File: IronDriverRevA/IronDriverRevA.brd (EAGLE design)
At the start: 100 x 100 mm, 46 parts, among them IC1 PIC18F2550, IC2 TL074P, IC3 7805TV, IC4 TL072P, IC5 MC34063AP, Q1 BC557C

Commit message: Finalizando Roteamento
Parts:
- added JMP1, JMP2, JMP3, JMP4, JMP5, JMP6, JMP7: (no value), rcl:R1206
- moved R9 26.6 mm to (60.7, 51.3), turned to 270 degrees
- moved ICSP 17.9 mm to (78.8, 56.0)
- moved R8 15.0 mm to (51.4, 37.1)
- moved IC2 15.0 mm to (51.4, 47.9)
- moved R10 14.4 mm to (60.7, 41.6)
- moved R7 14.4 mm to (58.1, 46.6)
- moved J1 14.2 mm to (90.6, 33.0)
- moved C1 13.4 mm to (85.6, 30.0)
- moved IC1 13.1 mm to (78.8, 35.0)
- moved R6 13.1 mm to (69.7, 47.8)
- moved R5 11.0 mm to (47.6, 25.0), turned to 270 degrees
- moved R3 7.94 mm to (50.1, 25.0), turned to 90 degrees
- moved PTC 7.03 mm to (5.85, 46.0)
- moved IC4 7.03 mm to (23.0, 51.0)
- moved Q1 7.03 mm to (34.5, 51.2)
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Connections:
- removed net LCD_D4: IC1.3
- removed net LCD_D5: IC1.5
- removed net LCD_D6: IC1.6
- removed net LCD_D7: IC1.7
- new net +5V_JMP4: J1.P$5, JMP4.1, R6.2
- new net +5V_MC: C1.1, IC1.20, JMP3.1
- new net GND_JMP5: J1.P$3, JMP5.1
- new net N$17: J1.P$6, JMP1.2
- new net N$23: J1.P$9, JMP7.2
- new net N$24: JMP6.2, JMP7.1
- new net ZEROCROSSING_B: JMP2.1, OPTO1.5, OPTO2.5, R3.1
- net +5V: now also JMP3.2, JMP4.2; no longer C1.1, IC1.20, J1.P$5, R6.2
- net ENC_B: now also JMP1.1; no longer J1.P$6
- net GND: now also JMP5.2; no longer J1.P$3
- net LCD_BL: now also IC1.25
- net LCD_D0: now also IC1.12
- net LCD_D1: now also IC1.17
- net LCD_D2: now also IC1.3
- net LCD_D3: now also IC1.26, JMP6.1; no longer J1.P$9
- net LCD_E: now also IC1.13; no longer IC1.18
- net LCD_RS: now also IC1.24; no longer IC1.17
- net LCD_RW: now also IC1.18; no longer IC1.13
- net ZEROCROSSING: now also JMP2.2; no longer OPTO1.5, OPTO2.5, R3.1
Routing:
- net GND: track 336.0 -> 413.4 mm
- net +5V: track 10.9 -> 63.3 mm
- net +5V_JMP4: track 0.00 -> 42.4 mm
- net LCD_D2: track 0.00 -> 40.0 mm
- net ZEROCROSSING_B: track 0.00 -> 33.7 mm
- net HEATER: track 0.00 -> 29.9 mm
- net ZEROCROSSING: track 18.1 -> 44.6 mm
- net GND_JMP5: track 0.00 -> 24.4 mm
- net LCD_D3: track 0.00 -> 21.2 mm
- net +PTC: track 55.4 -> 75.7 mm
- net LCD_E: track 0.00 -> 20.2 mm
- net LCD_D0: track 0.00 -> 19.0 mm
- net ENC_B: track 22.2 -> 4.09 mm
- net N$6: track 24.5 -> 7.59 mm
- net LCD_RW: track 24.6 -> 8.48 mm
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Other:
- board size 100 x 100 mm -> 100 x 60 mm
- board text added: "10/2014"
- board text added: "IronDriver"
- board text added: "Iuri C."
- board text added: "RevA"
- board text removed: "Subir MOC e OPTOS"

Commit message: Ajustes de trilhas
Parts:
- L2: device rcl:6000-XXXX-RC -> rcl:0204/7
- moved L2 1.35 mm to (66.5, 19.2), turned to 270 degrees
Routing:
- net N$16: track 18.0 -> 24.1 mm
- net +8V: track 132.7 -> 128.1 mm
- net GND: track 413.4 -> 412.4 mm
- net +5V: track 63.3 -> 62.5 mm

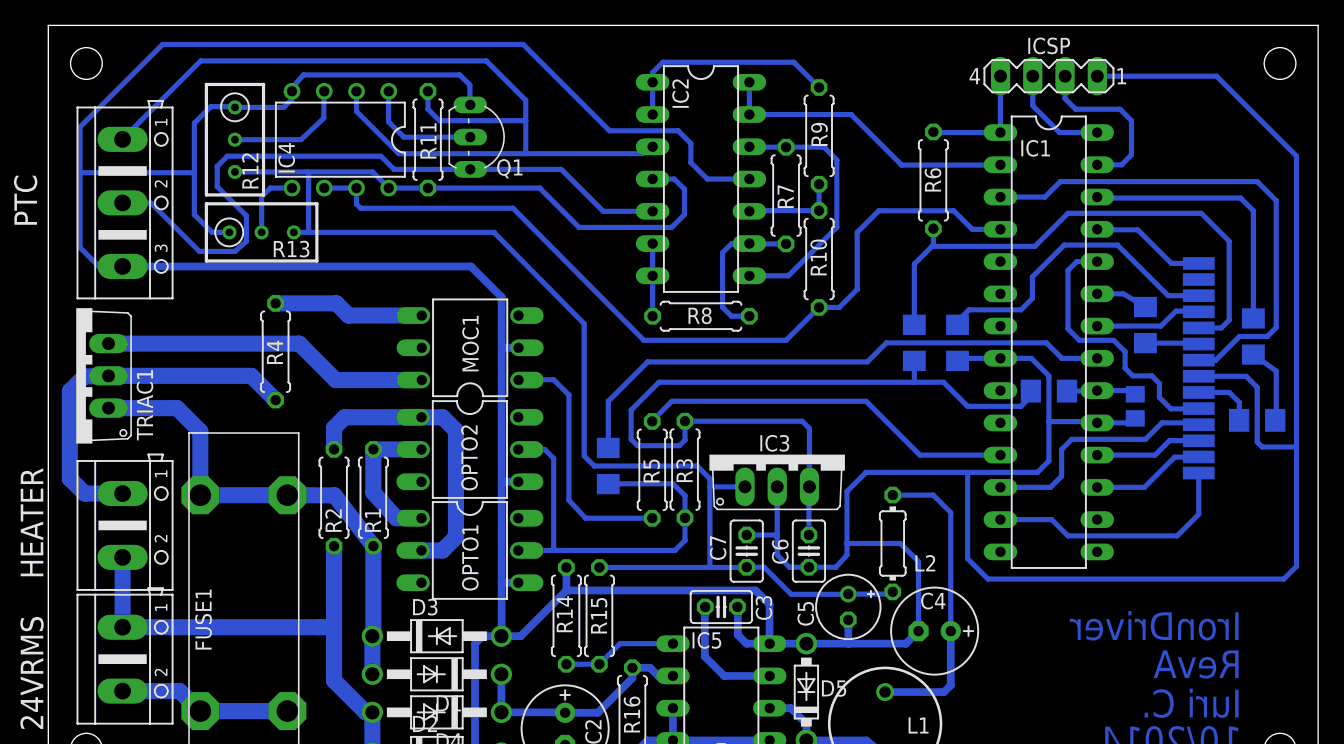
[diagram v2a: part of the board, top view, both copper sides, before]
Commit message: Alterado largura das trilhas
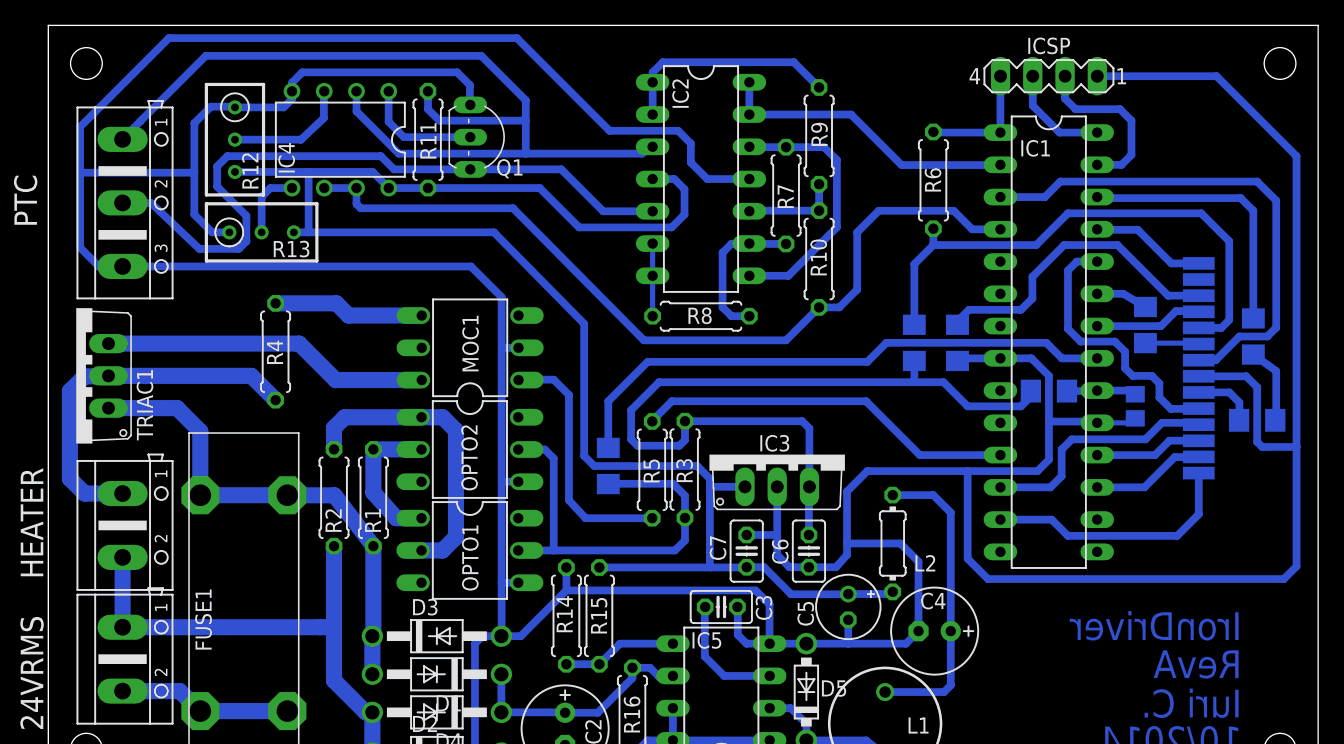
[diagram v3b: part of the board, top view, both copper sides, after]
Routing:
- net GND: track 412.4 -> 413.2 mm

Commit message: Ajustes
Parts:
- C2, C4: device rcl:E2,5-7 -> rcl:E3,5-8
- C5: device rcl:E2-5 -> rcl:E3,5-8
- moved L2 10.3 mm to (73.4, 11.6), turned to 180 degrees
- moved C4 8.79 mm to (74.7, 5.00), turned to 90 degrees
- moved C5 1.84 mm to (64.8, 13.8)
- moved D1 0.89 mm to (29.8, 8.50)
- moved D2 0.89 mm to (29.8, 2.30)
- moved D3 0.89 mm to (29.8, 11.5)
- moved D4 0.89 mm to (29.8, 5.50)
- moved C2 0.63 mm to (40.1, 4.40)
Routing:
- net GND: track 413.2 -> 421.9 mm, vias 0 -> 5
- net +8V: track 128.1 -> 133.9 mm, vias 0 -> 1
- net N$16: track 24.1 -> 20.0 mm
- net N$2: track 9.34 -> 7.94 mm, vias 0 -> 1
- net ZEROCROSSING_B: track 33.7 -> 32.4 mm
- net N$20: track 18.8 -> 20.0 mm, vias 0 -> 2
- net +PTC: track 76.1 -> 75.2 mm, vias 0 -> 1
- net LIVE: track 38.7 -> 39.5 mm
- net NEUTRAL: track 40.0 -> 40.6 mm, vias 0 -> 1
- net -PTC: track 54.9 -> 55.5 mm
- net N$5: vias 0 -> 1
- net N$4: vias 0 -> 1
- net N$15: vias 0 -> 1
- net N$13: vias 0 -> 1
- net +5V: vias 0 -> 1
